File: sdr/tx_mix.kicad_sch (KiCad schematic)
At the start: 3 parts, among them U10 74HCT00

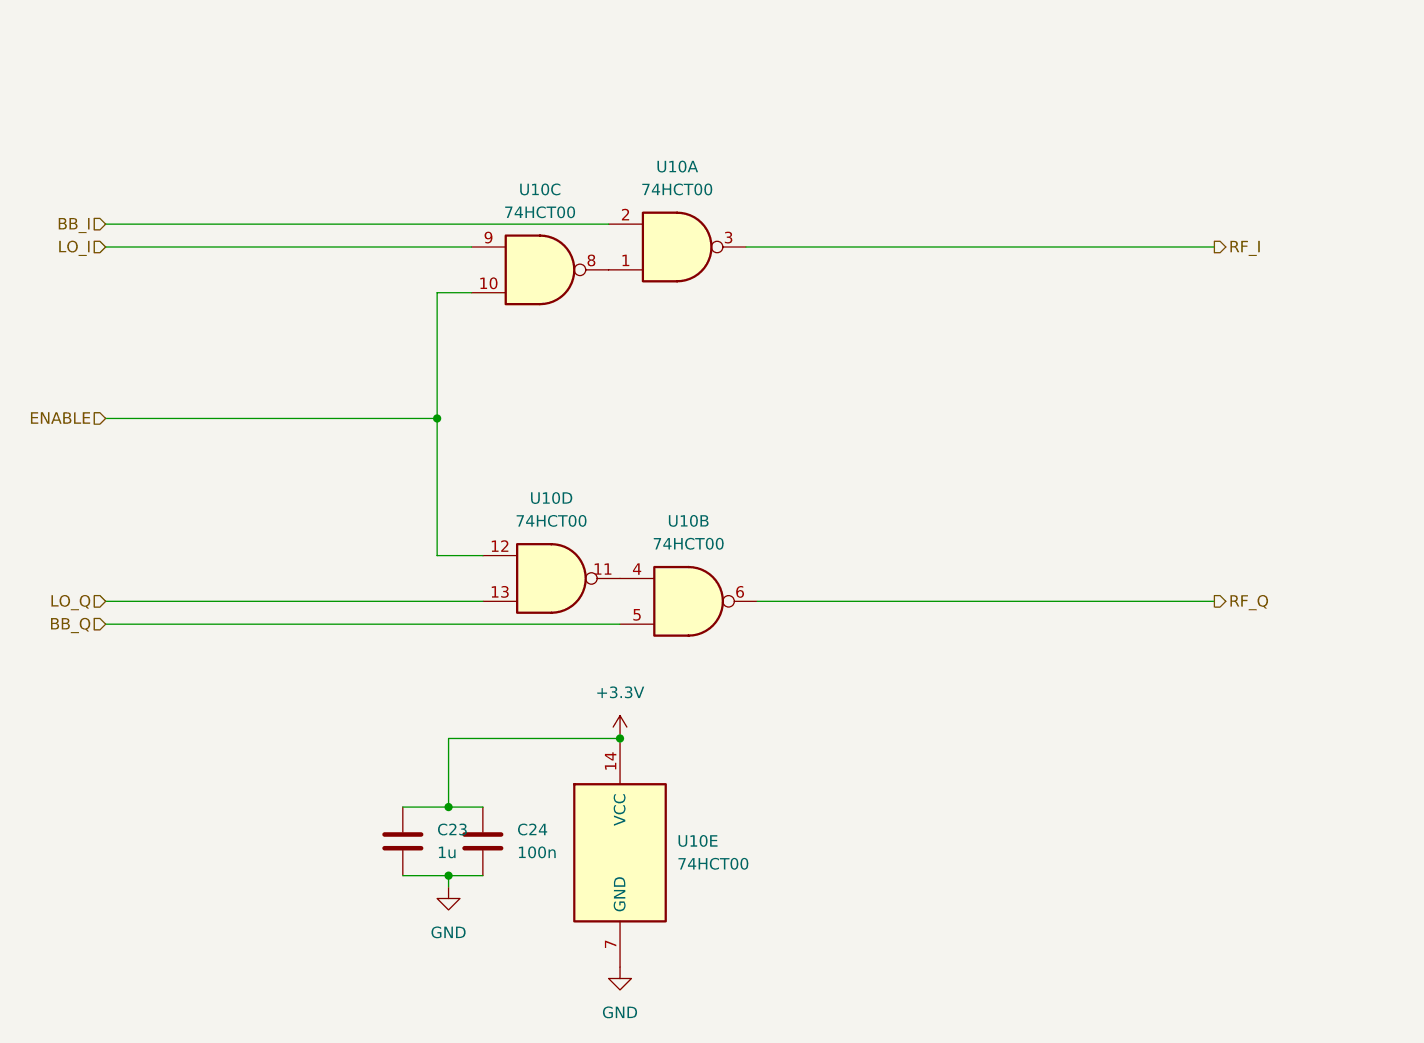
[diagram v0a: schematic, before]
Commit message: Many fixes. Updated mixers to use the analog switches rather than discretes.
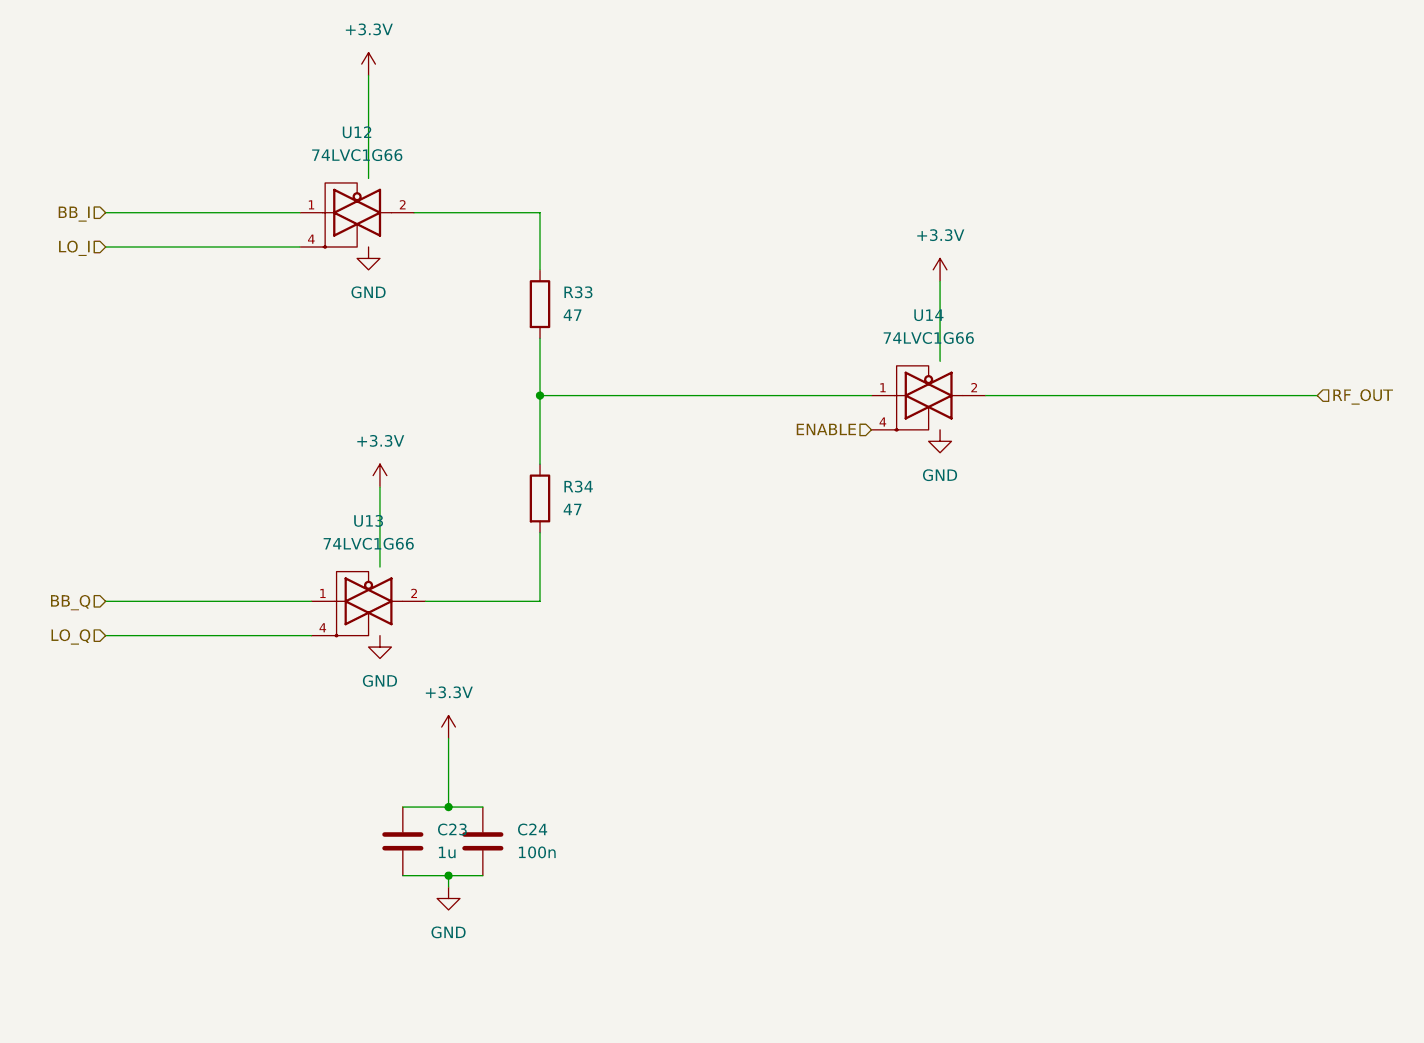
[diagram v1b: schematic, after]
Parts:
- removed U10: 74HCT00, symbol 74xx:74HCT00
- added R33, R34: 47, symbol Device:R
- added U12, U13, U14: 74LVC1G66, Package_TO_SOT_SMD:SOT-353_SC-70-5, symbol 74xGxx:74LVC1G66
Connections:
- net +3.3V: now also U12.5 (VCC), U13.5 (VCC), U14.5 (VCC)
- net BB_I: now also U12.1
- net BB_Q: now also U13.1
- net ENABLE: now also U14.4
- net GND: now also U12.3 (GND), U13.3 (GND), U14.3 (GND)
- net LO_I: now also U12.4
- net LO_Q: now also U13.4
- new net: R33.1, U12.2
- new net: R34.2, U13.2
- new net: R33.2, R34.1, U14.1
- new net RF_OUT: U14.2
